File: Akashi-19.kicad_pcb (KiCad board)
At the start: 2 copper layers, 111.8 x 95.9 mm, 7 parts, among them J1 Conn_01x20_Socket, J2 Conn_01x20_Socket, J3 GROVE I2C, J4 QWIIC, J5 SERIAL, SW1 RESET, U1 Raspberry Pi Pico

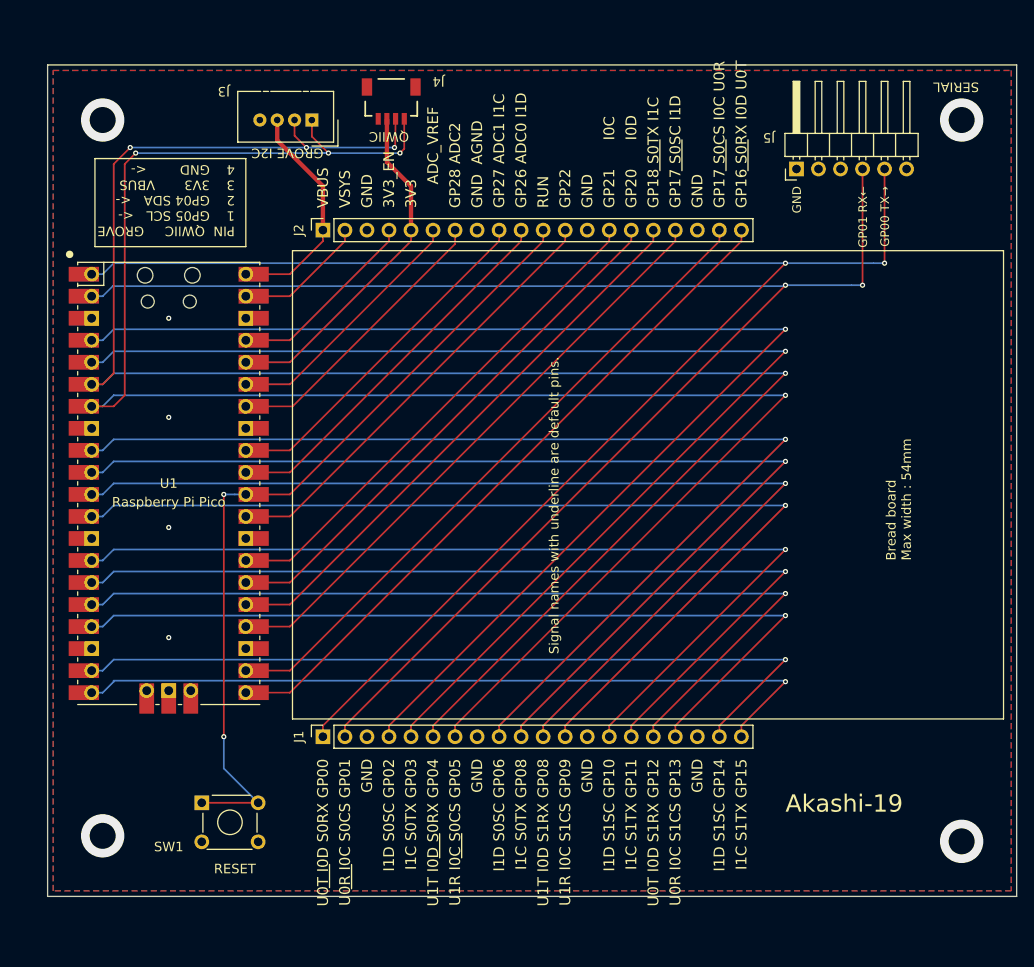
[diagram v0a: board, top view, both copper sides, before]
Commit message: Refine the size comment.
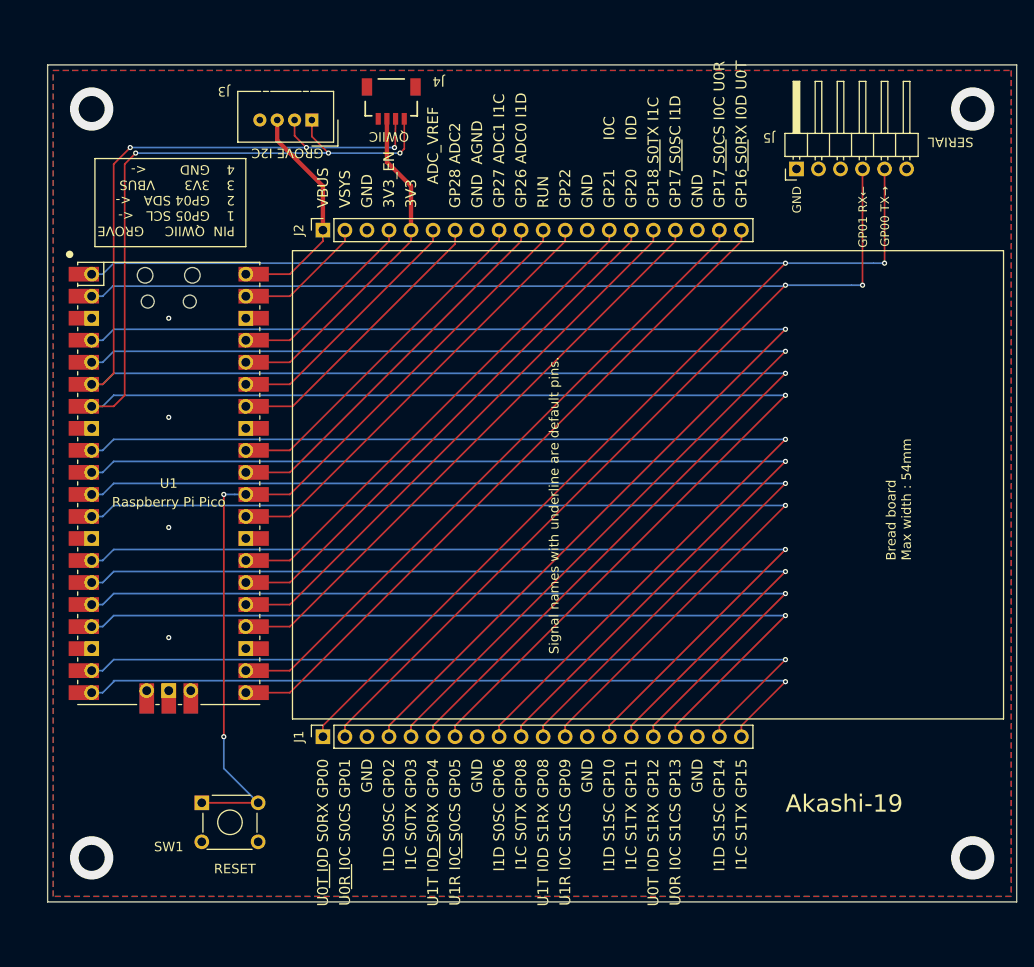
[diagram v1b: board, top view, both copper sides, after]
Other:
- board size 111.8 x 95.9 mm -> 111.8 x 96.5 mm
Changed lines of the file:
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@@
         (effects (font (size 1.1 1.1) (thickness 0.15)))
     )
-    (fp_text value "SERIAL" (at 9.455 18.415 180 unlocked) (layer "F.SilkS")
+    (fp_text value "SERIAL" (at 3.105 17.78 180 unlocked) (layer "F.SilkS")
         (effects (font (size 1.1 1.1) (thickness 0.15)))
     )
@@
   (gr_line (start 209.55 52.07) (end 97.79 52.07)
     (stroke (width 0.05) (type default)) (layer "Edge.Cuts"))
-  (gr_line (start 97.79 147.955) (end 209.55 147.955)
+  (gr_line (start 97.79 148.59) (end 209.55 148.59)
     (stroke (width 0.05) (type default)) (layer "Edge.Cuts"))
-  (gr_line (start 97.79 52.07) (end 97.79 147.955)
+  (gr_line (start 97.79 52.07) (end 97.79 148.59)
     (stroke (width 0.05) (type default)) (layer "Edge.Cuts"))
-  (gr_line (start 209.55 147.955) (end 209.55 52.07)
+  (gr_line (start 209.55 148.59) (end 209.55 52.07)
     (stroke (width 0.05) (type default)) (layer "Edge.Cuts"))
   (gr_text "Raspberry Pi Pico Breadboard. v1.0.0\n(C) Seiichi Horie, 2024\nhttps://github.com/suikan4github/Akashi-19" (at 195.58 142.24) (layer "B.SilkS")
@@
   )
   (dimension (type aligned) (layer "Cmts.User")
-    (pts (xy 209.55 147.955) (xy 209.55 52.07))
+    (pts (xy 209.55 148.59) (xy 209.55 52.07))
     (height 8.255)
-    (gr_text "95.8850 mm" (at 216.555 100.0125 90) (layer "Cmts.User")
+    (gr_text "96.5200 mm" (at 216.555 100.33 90) (layer "Cmts.User")
       (effects (font (size 1.1 1.1) (thickness 0.15)))
     )
@@
   )
   (dimension (type aligned) (layer "Cmts.User")
-    (pts (xy 203.2 141.605) (xy 209.55 141.605))
+    (pts (xy 204.47 141.605) (xy 209.55 141.605))
     (height 9.525)
-    (gr_text "6.3500 mm" (at 206.375 149.98) (layer "Cmts.User")
+    (gr_text "5.0800 mm" (at 207.01 149.98) (layer "Cmts.User")
       (effects (font (size 1 1) (thickness 0.15)))
     )
@@
   )
   (dimension (type aligned) (layer "Cmts.User")
-    (pts (xy 104.14 140.97) (xy 104.14 58.42))
-    (height -11.43)
-    (gr_text "82.5500 mm" (at 91.46 99.695 90) (layer "Cmts.User")
-      (effects (font (size 1.1 1.1) (thickness 0.15)))
-    )
-    (format (prefix "") (suffix "") (units 3) (units_format 1) (precision 4))
-    (style (thickness 0.1) (arrow_length 1.27) (text_position_mode 0) (extension_height 0.58642) (extension_offset 0.5) keep_text_aligned)
-  )
-  (dimension (type aligned) (layer "Cmts.User")
-    (pts (xy 203.2 58.42) (xy 104.14 58.42))
-    (height 9.525)
-    (gr_text "99.0600 mm" (at 153.67 47.645) (layer "Cmts.User")
+    (pts (xy 97.79 147.32) (xy 209.55 147.32))
+    (height 10.16)
+    (gr_text "111.7600 mm" (at 153.67 156.23) (layer "Cmts.User")
       (effects (font (size 1.1 1.1) (thickness 0.15)))
     )
@@
   )
   (dimension (type aligned) (layer "Cmts.User")
-    (pts (xy 97.79 147.32) (xy 209.55 147.32))
-    (height 6.35)
-    (gr_text "111.7600 mm" (at 153.67 152.42) (layer "Cmts.User")
-      (effects (font (size 1.1 1.1) (thickness 0.15)))
+    (pts (xy 202.565 143.51) (xy 202.565 148.59))
+    (height -12.065)
+    (gr_text "5.0800 mm" (at 213.48 146.05 90) (layer "Cmts.User")
+      (effects (font (size 1 1) (thickness 0.15)))
     )
     (format (prefix "") (suffix "") (units 3) (units_format 1) (precision 4))
@@
   )
   (dimension (type aligned) (layer "Cmts.User")
-    (pts (xy 203.2 141.605) (xy 203.2 147.955))
-    (height -12.065)
-    (gr_text "6.3500 mm" (at 214.115 144.78 90) (layer "Cmts.User")
+    (pts (xy 102.87 58.42) (xy 97.79 58.42))
+    (height 9.525)
+    (gr_text "5.0800 mm" (at 100.33 47.745) (layer "Cmts.User")
       (effects (font (size 1 1) (thickness 0.15)))
     )
@@
   )
   (dimension (type aligned) (layer "Cmts.User")
-    (pts (xy 104.14 58.42) (xy 97.79 58.42))
-    (height 9.525)
-    (gr_text "6.3500 mm" (at 100.965 47.745) (layer "Cmts.User")
+    (pts (xy 208.03 127.49) (xy 126.03 127.49))
+    (height -27.45)
+    (gr_text "82.0000 mm" (at 167.03 153.79) (layer "Cmts.User")
       (effects (font (size 1 1) (thickness 0.15)))
     )
@@
   )
   (dimension (type aligned) (layer "Cmts.User")
-    (pts (xy 104.14 58.42) (xy 104.14 52.07))
+    (pts (xy 104.14 57.15) (xy 104.14 52.07))
     (height -11.43)
-    (gr_text "6.3500 mm" (at 91.56 55.245 90) (layer "Cmts.User")
+    (gr_text "5.0800 mm" (at 91.56 54.61 90) (layer "Cmts.User")
       (effects (font (size 1 1) (thickness 0.15)))
     )
@@
   (segment (start 170.18 71.12) (end 170.18 72.39) (width 0.2) (layer "F.Cu") (net 17))
   (via (at 111.76 81.28) (size 0.6) (drill 0.3) (layers "F.Cu" "B.Cu") (free) (net 18))
-  (via locked (at 104.14 58.42) (size 5) (drill 3) (layers "F.Cu" "B.Cu") (free) (net 18))
-  (via locked (at 203.2 58.42) (size 5) (drill 3) (layers "F.Cu" "B.Cu") (free) (net 18))
-  (via locked (at 203.2 141.605) (size 5) (drill 3) (layers "F.Cu" "B.Cu") (free) (net 18))
-  (via locked (at 104.14 140.97) (size 5) (drill 3) (layers "F.Cu" "B.Cu") (free) (net 18))
+  (via (at 102.87 57.15) (size 5) (drill 3) (layers "F.Cu" "B.Cu") (free) (net 18))
+  (via locked (at 204.47 57.15) (size 5) (drill 3) (layers "F.Cu" "B.Cu") (free) (net 18))
+  (via locked (at 204.47 143.51) (size 5) (drill 3) (layers "F.Cu" "B.Cu") (free) (net 18))
+  (via locked (at 102.87 143.51) (size 5) (drill 3) (layers "F.Cu" "B.Cu") (free) (net 18))
   (via (at 111.76 92.71) (size 0.6) (drill 0.3) (layers "F.Cu" "B.Cu") (free) (net 18))
   (via (at 111.76 105.41) (size 0.6) (drill 0.3) (layers "F.Cu" "B.Cu") (free) (net 18))
@@
       (pts
         (xy 208.915 52.705)
-        (xy 208.915 147.32)
-        (xy 98.425 147.32)
+        (xy 208.915 147.955)
+        (xy 98.425 147.955)
         (xy 98.425 52.705)
       )
@@
       (pts
         (xy 208.915 52.705)
-        (xy 208.915 147.32)
-        (xy 98.425 147.32)
+        (xy 208.915 147.955)
+        (xy 98.425 147.955)
         (xy 98.425 52.705)
       )

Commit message: Correct the wrong connection of Qwiic.
The connection was right-side-left.
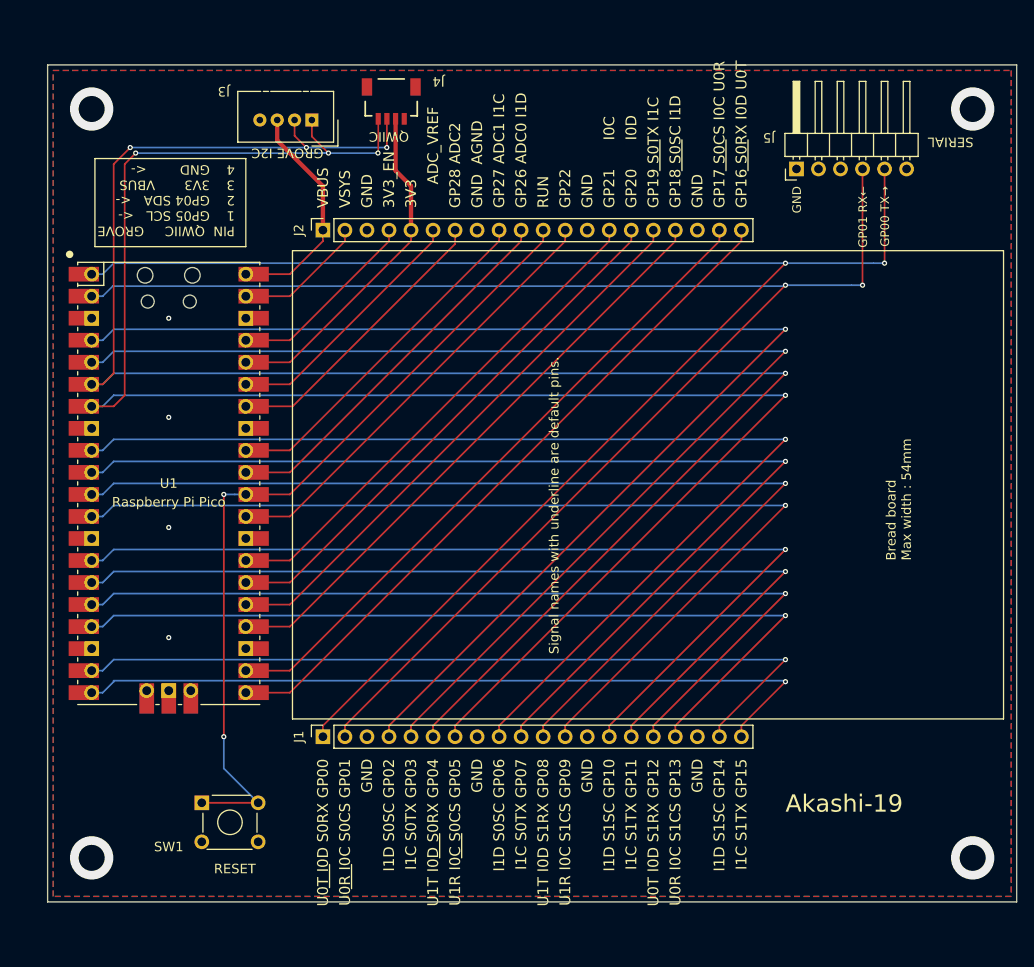
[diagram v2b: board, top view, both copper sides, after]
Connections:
- J4 pad 1: /SCL -> GND
- J4 pad 2: /SDA -> +3.3V
- J4 pad 3: +3.3V -> /SDA
- J4 pad 4: GND -> /SCL
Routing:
- net /SCL: track 209.0 -> 206.3 mm
- net /SDA: track 206.8 -> 205.8 mm
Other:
- board text added: "GP18 S0SC I1D"
- board text added: "GP19 S0TX I1C"
- board text added: "I1C S0TX GP07"
- board text removed: "GP17 S0SC I1D"
- board text removed: "GP18 S0TX I1C"
- board text removed: "I1C S0TX GP08"

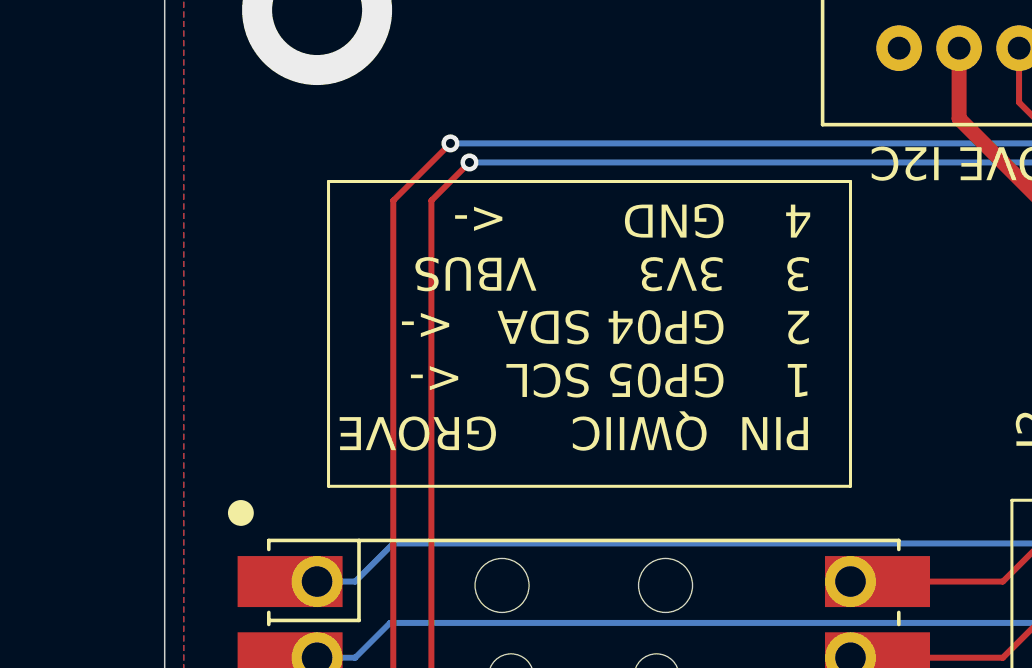
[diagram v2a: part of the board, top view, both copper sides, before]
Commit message: Correct the wrong description of QWIIC.
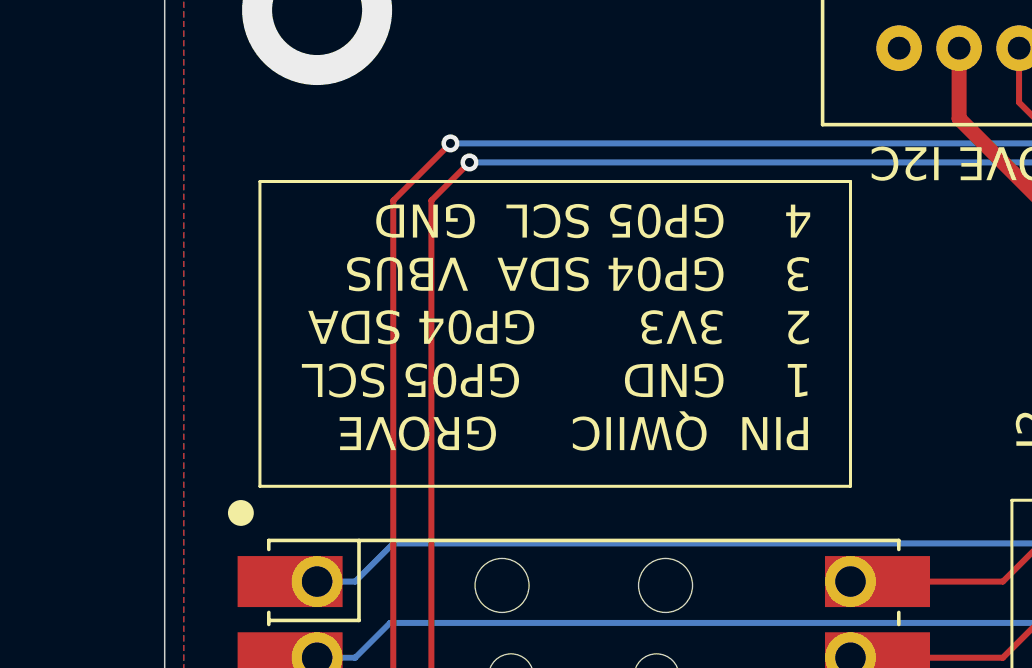
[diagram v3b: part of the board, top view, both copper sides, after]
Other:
- board text added: "PIN QWIIC GROVE 1 GND GP05 SCL 2 3V3 GP04 SDA 3 GP04 SDA VBUS 4 GP05 SCL GND"
- board text removed: "PIN QWIIC GROVE 1 GP05 SCL <- 2 GP04 SDA <- 3 3V3 VBUS 4 GND <-"
